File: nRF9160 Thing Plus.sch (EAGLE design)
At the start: 91 parts, among them J1 USB Female C, J10 QWIIC_RIGHT_ANGLE, J2 CON-HEADER-1X12-MALE-PIN, J3 CON-HEADER-1X16-MALE-PIN, J4 CON-1909763-1, J7 CON-1909763-1, J9 CON-0002, P1 CON-SIM-SF72S006VBAR2500, Q1 MOSFET-P-SC89, Q2 MOSFET-DUAL-COMP-SOT563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

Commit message: Updated name label and eSIM cream
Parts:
- U10: device wolff-den:IC-SIM-ST-MFF2 -> nrF9160 Thing Plus temp:IC-SIM-ST-MFF2NO_CREAM
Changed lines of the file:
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@@
 <?xml version="1.0" encoding="utf-8"?>
 <!DOCTYPE eagle SYSTEM "eagle.dtd">
-<eagle version="9.5.1">
+<eagle version="9.5.2">
 <drawing>
 <settings>
-<setting alwaysvectorfont="no"/>
+<setting alwaysvectorfont="yes"/>
 <setting keepoldvectorfont="yes"/>
 <setting verticaltext="up"/>
@@
 <layer number="128" name="_bValues" color="7" fill="1" visible="yes" active="yes"/>
 <layer number="129" name="Mask" color="7" fill="1" visible="no" active="yes"/>
+<layer number="130" name="SMDSTROOK" color="7" fill="1" visible="no" active="no"/>
 <layer number="131" name="tAdjust" color="7" fill="1" visible="no" active="yes"/>
 <layer number="132" name="bAdjust" color="7" fill="1" visible="no" active="yes"/>
+<layer number="133" name="bottom_silk" color="7" fill="1" visible="no" active="no"/>
+<layer number="134" name="mbFinish" color="7" fill="1" visible="no" active="no"/>
 <layer number="135" name="_tanames" color="7" fill="1" visible="no" active="yes"/>
 <layer number="136" name="_banames" color="7" fill="1" visible="no" active="yes"/>
 <layer number="137" name="_taDocu" color="7" fill="1" visible="no" active="yes"/>
 <layer number="138" name="_baDocu" color="7" fill="1" visible="no" active="yes"/>
+<layer number="139" name="mtKeepout" color="7" fill="1" visible="no" active="no"/>
+<layer number="140" name="mbKeepout" color="7" fill="1" visible="no" active="no"/>
+<layer number="141" name="mtRestrict" color="7" fill="1" visible="no" active="no"/>
+<layer number="142" name="mbRestrict" color="7" fill="1" visible="no" active="no"/>
+<layer number="143" name="mvRestrict" color="7" fill="1" visible="no" active="no"/>
 <layer number="144" name="Drill_legend" color="7" fill="1" visible="yes" active="yes"/>
 <layer number="145" name="DrillLegend_01-16" color="2" fill="9" visible="no" active="yes"/>
+<layer number="146" name="mMilling" color="7" fill="1" visible="no" active="no"/>
+<layer number="147" name="mMeasures" color="7" fill="1" visible="no" active="no"/>
+<layer number="148" name="mDocument" color="7" fill="1" visible="no" active="no"/>
+<layer number="149" name="mReference" color="7" fill="1" visible="no" active="no"/>
 <layer number="150" name="Notes" color="7" fill="1" visible="yes" active="yes"/>
 <layer number="151" name="HeatSink" color="7" fill="1" visible="yes" active="yes"/>
@@
 <layer number="154" name="FabDoc2" color="2" fill="1" visible="no" active="no"/>
 <layer number="155" name="FabDoc3" color="7" fill="15" visible="no" active="no"/>
+<layer number="191" name="mNets" color="7" fill="1" visible="no" active="no"/>
+<layer number="192" name="mBusses" color="7" fill="1" visible="no" active="no"/>
+<layer number="193" name="mPins" color="7" fill="1" visible="no" active="no"/>
+<layer number="194" name="mSymbols" color="7" fill="1" visible="no" active="no"/>
+<layer number="195" name="mNames" color="7" fill="1" visible="no" active="no"/>
+<layer number="196" name="mValues" color="7" fill="1" visible="no" active="no"/>
 <layer number="199" name="Contour" color="7" fill="1" visible="yes" active="yes"/>
 <layer number="200" name="200bmp" color="1" fill="10" visible="yes" active="yes"/>
@@
 <layer number="255" name="routoute" color="7" fill="1" visible="yes" active="yes"/>
 </layers>
-<schematic xreflabel="%F%N/%S.%C%R" xrefpart="/%S.%C%R">
+<schematic xreflabel="%F%N/%S" xrefpart="/%S.%C%R">
 <attributes>
 <attribute name="AUTHOR" value="Jared Wolff"/>
@@
 <part name="U7" library="wolff-den" library_urn="urn:adsk.eagle:library:6370453" deviceset="IC-NX3DV2567GU" device=""/>
 <part name="GND47" library="supply1" library_urn="urn:adsk.eagle:library:371" deviceset="GND" device=""/>
-<part name="U10" library="wolff-den" library_urn="urn:adsk.eagle:library:6370453" deviceset="IC-SIM-ST-MFF2" device=""/>
+<part name="U10" library="nrF9160 Thing Plus temp" deviceset="IC-SIM-ST-MFF2" device="NO_CREAM" value="IC-SIM-ST-MFF2"/>
 <part name="GND48" library="supply1" library_urn="urn:adsk.eagle:library:371" deviceset="GND" device=""/>
 <part name="U11" library="wolff-den" library_urn="urn:adsk.eagle:library:6370453" deviceset="IC-EMIF03-SIM02M8" device=""/>

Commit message: Moved components to local libraries
Parts not in SFE Eagle libraries were moved to local temporary libraries with the SFE SKUs added for the BOM
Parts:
- C1, C2: device wolff-den:CAP-15P-50V-0402 -> nRF9160-Capacitors:CAP-15P-50V-0402
- C10, C13, C15, C3, C8, C9: device wolff-den:CAP-4.7U-6.3V-2-0603 -> nRF9160-Capacitors:CAP-4.7U-6.3V-2-0603
- C11: device wolff-den:CAP-1U-25V-1-0402 -> nRF9160-Capacitors:CAP-1U-25V-1-0402
- C12, C19: device wolff-den:CAP-56PF-50V-1-0402 -> nRF9160-Capacitors:CAP-56PF-50V-0402
- C14, C16, C17, C18, C20, C6: device wolff-den:CAP-0.1U-50V-0402 -> nRF9160-Capacitors:CAP-0.1U-50V-0402
- C4, C5, C7: device wolff-den:CAP-10U-6.3V-0603 -> nRF9160-Capacitors:CAP-10U-6.3V-0603
- J4, J7: device wolff-den:CON-1909763-1 -> nRF9160-Connectors:CON-1909763-1
- L1: device wolff-den:IND-39NH-250MA-0402 -> nRF9160-Coils:IND-39NH-250MA-0402
- L2: device wolff-den:IND-1.5U-1.4A-2X2 -> nRF9160-Coils:IND-1.5U-1.4A-2X2
- L4: device wolff-den:IND-68NH-200MA-0402 -> nRF9160-Coils:IND-68NH-200MA-0402
- P1: device wolff-den:CON-SIM-SF72S006VBAR2500 -> nRF9160-Connectors:CON-SIM-SF72S006VBAR2500
- Q1: device wolff-den:MOSFET-P-SC89 -> nRF9160-DiscreteSemi:MOSFET-P-SC89
- Q2: device wolff-den:MOSFET-DUAL-COMP-SOT563 -> nRF9160-DiscreteSemi:MOSFET-DUAL-COMP-SOT563
- Q3: device wolff-den:MOSFET-P-20V-4.7A-SOT23 -> nRF9160-DiscreteSemi:MOSFET-P-20V-4.7A-SOT23
- Q4, Q5: device wolff-den:MOSFET-N-SC89 -> nRF9160-DiscreteSemi:MOSFET-N-SC89
- R1, R10, R13, R23, R3, R5, R6, R7, R8: device wolff-den:RES-100K-1%-0402 -> nRF9160-Resistors:RES-100K-1%-0402
- R11, R14: device wolff-den:RES-330-5%-0402 -> nRF9160-Resistors:RES-330-5%-0402
- R12: device wolff-den:RES-2K-1%-0402 -> nRF9160-Resistors:RES-2K-1%-0402
- R15: device wolff-den:RES-22K-1%-0402 -> nRF9160-Resistors:RES-22K-1%-0402
- R16: device wolff-den:RES-33K-1%-0402 -> nRF9160-Resistors:RES-33K-1%-0402
- R17, R18: device wolff-den:RES-10K-1%-0402 -> nRF9160-Resistors:RES-10K-1%-0402
- R19, R2, R22, R9: device wolff-den:RES-1M-5%-0402 -> nRF9160-Resistors:RES-1M-5%-0402
- R4: device wolff-den:RES-1K-5%-0402 -> nRF9160-Resistors:RES-1K-5%-0402
- U1: device wolff-den:MOD-NRF9160-SICA-R -> nRF9160-IC:MOD-NRF9160-SICA-R
- U11: device wolff-den:IC-EMIF03-SIM02M8 -> nRF9160-IC:IC-EMIF03-SIM02M8
- U12: device wolff-den:IC-LIS2DH12TR -> nRF9160-IC:IC-LIS2DH12TR
- U3: device wolff-den:IC-TPS63031DSKR -> nRF9160-IC:IC-TPS63031DSKR
- U4: device wolff-den:POWER-SWITCH-MIC94092YC6 -> nRF9160-IC:POWER-SWITCH-MIC94092YC6
- U5: device wolff-den:IC-CP2102N-A02-GQFN24R -> nRF9160-IC:IC-CP2102N-A02-GQFN24R
- U6: value FLASH-W25Q16JVZPIQ-WSON -> FLASH-W25Q128JVPIM-WSON; device wolff-den:FLASH-W25Q16JVZPIQ-WSON -> nRF9160-IC:FLASH-W25Q128JVPIM-WSON
- U7: device wolff-den:IC-NX3DV2567GU -> nRF9160-IC:IC-NX3DV2567GU
- U8: device wolff-den:IC-PCF85063ATL/1 -> nRF9160-IC:IC-PCF85063ATL/1
- U9: device wolff-den:IC-BAV70S -> nRF9160-DiscreteSemi:IC-BAV70S
- Y1: device wolff-den:XTAL-ABS07AIG-32.768KHZ-7-T -> nRF9160-Clocks:XTAL-ABS07AIG-32.768KHZ-7-T

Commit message: Adding Cortex-m header. Removing tag connect. Removing external SIM bits. Changing SIM holder to cheaper variant.
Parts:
- removed C18: 0.1u, nRF9160-Capacitors:CAP-0.1U-50V-0402
- removed J9: CON-0002, wolff-den:CON-0002
- removed P1: CON-SIM-SF72S006VBAR2500, nRF9160-Connectors:CON-SIM-SF72S006VBAR2500
- removed R22: 1M, nRF9160-Resistors:RES-1M-5%-0402
- removed SOLDER1: SOLDER-PASTE-ROOM-TEMP-50G, wolff-den:SOLDER-PASTE-ROOM-TEMP-50G
- removed U$34: FIDUCIAL-1MM, wolff-den:FIDUCIAL-1MM
- removed U10: IC-SIM-ST-MFF2, nrF9160 Thing Plus temp:IC-SIM-ST-MFF2NO_CREAM
- removed U11: IC-EMIF03-SIM02M8, nRF9160-IC:IC-EMIF03-SIM02M8
- removed U7: IC-NX3DV2567GU, nRF9160-IC:IC-NX3DV2567GU
- added J6: CON-SIM-104224-0820, wolff-den:CON-SIM-104224-0820
- added J8: CON-FTSH-105-XX-X-DV, wolff-den:CON-FTSH-105-XX-X-DV
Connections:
- removed net SIM_EMB_CLK: U10.CLK, U7.3Y1
- removed net SIM_EMB_IO: U10.I/O, U7.4Y1
- removed net SIM_EMB_RST: U10.RST, U7.2Y1
- removed net SIM_EMB_VCC: U10.VCC, U7.1Y1
- removed net SIM_HLDR_CLK: U11.CLKIN, U7.3Y0
- removed net SIM_HLDR_CLK_F: P1.CLK, U11.CLKEXT
- removed net SIM_HLDR_IO: U11.DATAIN, U7.4Y0
- removed net SIM_HLDR_IO_F: P1.I/O, U11.DATAEXT
- removed net SIM_HLDR_RST: U11.RSTIN, U7.2Y0
- removed net SIM_HLDR_RST_F: P1.RST, U11.RSTEXT
- removed net SIM_HLDR_VCC: P1.VCC, U11.VCC, U7.1Y0
- net +3V3: now also J8.VCC; no longer J9.VCC
- net GND: now also J6.GND, J8.GND; no longer C18.2, J9.GND, P1.DSW, P1.GND, P1.SHIELD, U10.EPAD, U10.GND, U11.GND, U7.GND
- net SIM_CLK: now also J6.CLK; no longer U7.3Z
- net SIM_DET: no longer P1.CSW, R22.2, U7.IN
- net SIM_IO: now also J6.I/O; no longer U7.4Z
- net SIM_RST: now also J6.RST; no longer U7.2Z
- net SIM_VCC: now also J6.VCC; no longer C18.1, R22.1, U7.1Z, U7.VCC
- net SWCLK: now also J8.SWDCLK; no longer J9.SWCLK
- net SWDIO: now also J8.SWDIO; no longer J9.SWDIO
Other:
- note added: "Nano SIM"
- note removed: "SIMs"
- moved on the sheet: TP1, TP2

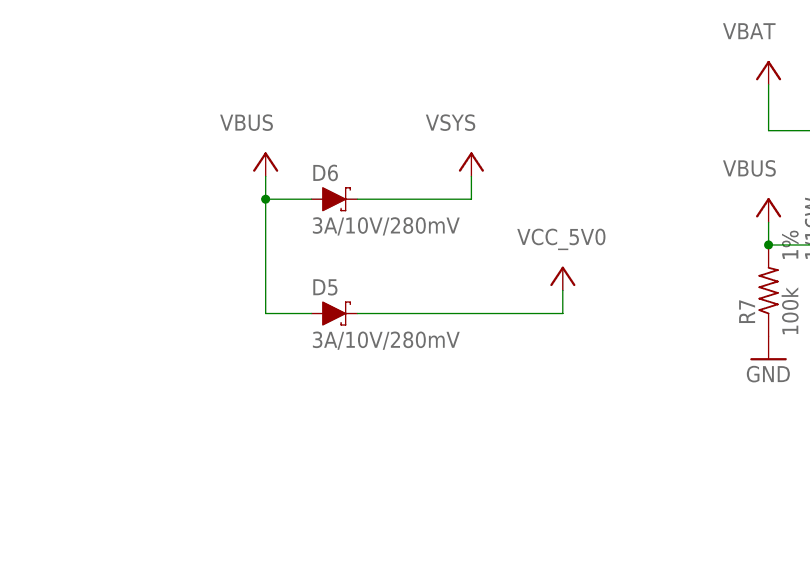
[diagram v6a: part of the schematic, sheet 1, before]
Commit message: Changing flash to W25Q32JVZPIQ. Changing D5/6 to BAT20J.
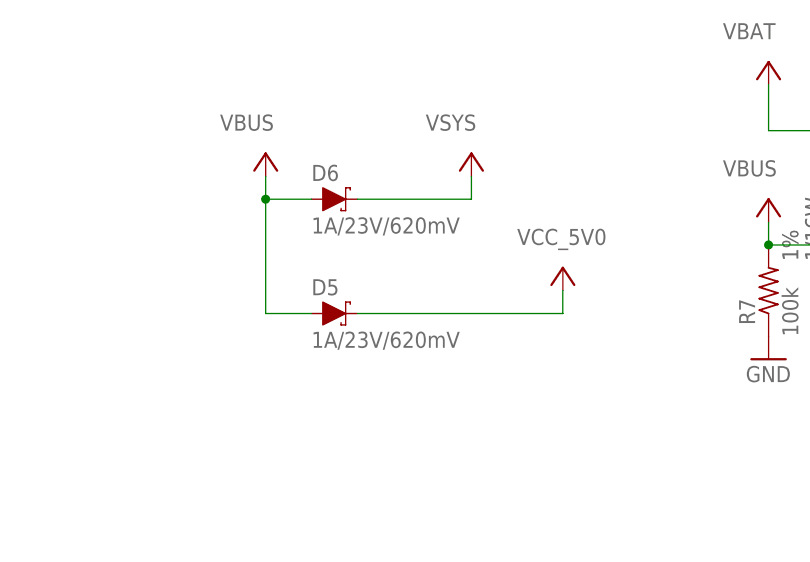
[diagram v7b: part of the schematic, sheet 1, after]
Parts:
- D5, D6: value 3A/10V/280mV -> 1A/23V/620mV; device SparkFun-DiscreteSemi:DIODE-SCHOTTKY-BAT60A -> SparkFun-DiscreteSemi:DIODE-SCHOTTKY-BAT20J
- U6: value FLASH-W25Q128JVPIM-WSON -> FLASH-WSON; device nRF9160-IC:FLASH-W25Q128JVPIM-WSON -> wolff-den:FLASH-W25Q32JVZPIQ-WSON
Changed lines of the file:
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@@
 <?xml version="1.0" encoding="utf-8"?>
 <!DOCTYPE eagle SYSTEM "eagle.dtd">
-<eagle version="9.5.1">
+<eagle version="9.6.2">
 <drawing>
 <settings>
@@
 <part name="SW2" library="SparkFun-Switches" deviceset="MOMENTARY-SWITCH-SPST" device="-SMD-4.6X2.8MM"/>
 <part name="GND13" library="supply1" library_urn="urn:adsk.eagle:library:371" deviceset="GND" device=""/>
-<part name="U6" library="nRF9160-IC" deviceset="FLASH" device="-WSON" package3d_urn="urn:adsk.eagle:package:19416409/2" override_package3d_urn="urn:adsk.eagle:package:19415944/2" override_package_urn="urn:adsk.eagle:footprint:19415945/1" override_locally_modified="yes" technology="-W25Q128JVPIM" value="FLASH-W25Q128JVPIM-WSON"/>
+<part name="U6" library="wolff-den" library_urn="urn:adsk.eagle:library:6370453" deviceset="FLASH" device="-WSON" package3d_urn="urn:adsk.eagle:package:19416409/2" override_package3d_urn="urn:adsk.eagle:package:19415944/2" override_package_urn="urn:adsk.eagle:footprint:19415945/1" override_locally_modified="yes" technology="-W25Q32JVZPIQ" value="FLASH-WSON"/>
 <part name="GND15" library="supply1" library_urn="urn:adsk.eagle:library:371" deviceset="GND" device=""/>
 <part name="+3V7" library="supply1" library_urn="urn:adsk.eagle:library:371" deviceset="+3V3" device=""/>
@@
 <part name="U5" library="nRF9160-IC" deviceset="IC-CP2102N-A02-GQFN24R" device=""/>
 <part name="J5" library="SparkFun-Connectors" library_urn="urn:adsk.eagle:library:513" deviceset="JST_2MM_MALE" device="" package3d_urn="urn:adsk.eagle:package:38042/1"/>
-<part name="D5" library="SparkFun-DiscreteSemi" deviceset="DIODE-SCHOTTKY" device="-BAT60A" value="3A/10V/280mV"/>
-<part name="D6" library="SparkFun-DiscreteSemi" deviceset="DIODE-SCHOTTKY" device="-BAT60A" value="3A/10V/280mV"/>
+<part name="D5" library="SparkFun-DiscreteSemi" deviceset="DIODE-SCHOTTKY" device="-BAT20J" value="1A/23V/620mV"/>
+<part name="D6" library="SparkFun-DiscreteSemi" deviceset="DIODE-SCHOTTKY" device="-BAT20J" value="1A/23V/620mV"/>
 <part name="U12" library="nRF9160-IC" deviceset="IC-LIS2DH12TR" device="" package3d_urn="urn:adsk.eagle:package:5807341/2" override_package3d_urn="urn:adsk.eagle:package:5807341/3" override_package_urn="urn:adsk.eagle:footprint:5807301/2"/>
 <part name="SUPPLY3" library="supply2" library_urn="urn:adsk.eagle:library:372" deviceset="GND" device=""/>

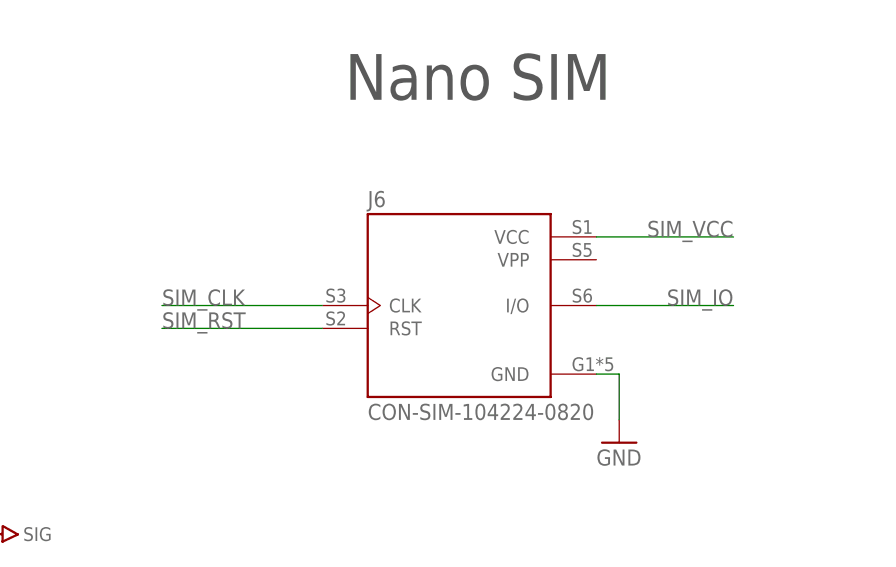
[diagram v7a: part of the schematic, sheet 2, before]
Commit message: Adding test points for SIM
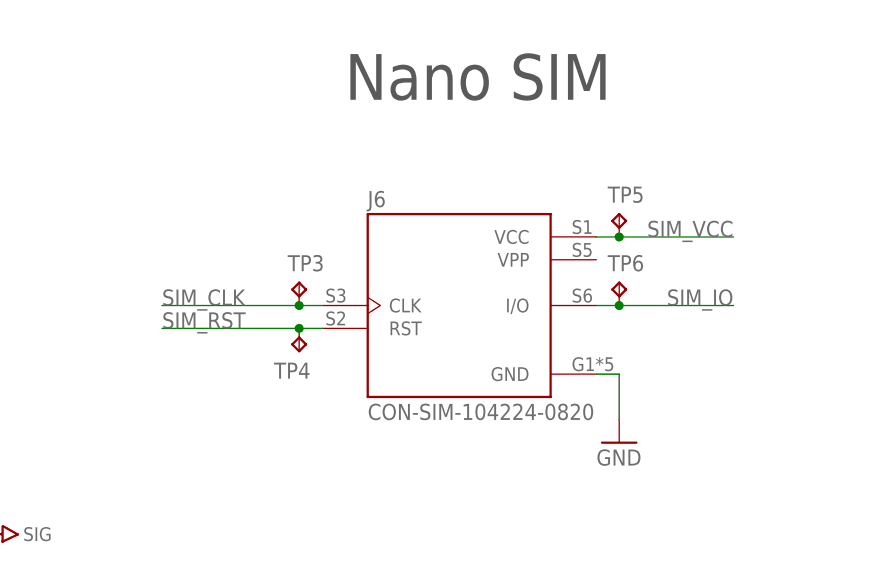
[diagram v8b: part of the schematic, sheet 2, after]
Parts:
- added TP3, TP4, TP5, TP6: TP-1SIDE-1P0, wolff-den:TP-1SIDE-1P0
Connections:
- net SIM_CLK: now also TP3.TP
- net SIM_IO: now also TP6.TP
- net SIM_RST: now also TP4.TP
- net SIM_VCC: now also TP5.TP
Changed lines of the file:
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@@
 <part name="GND32" library="supply1" library_urn="urn:adsk.eagle:library:371" deviceset="GND" device=""/>
 <part name="J6" library="wolff-den" library_urn="urn:adsk.eagle:library:6370453" deviceset="CON-SIM" device="" package3d_urn="urn:adsk.eagle:package:19415237/3" technology="-104224-0820"/>
+<part name="TP3" library="wolff-den" library_urn="urn:adsk.eagle:library:6370453" deviceset="TP" device="-1SIDE-1P0" package3d_urn="urn:adsk.eagle:package:24898411/1"/>
+<part name="TP4" library="wolff-den" library_urn="urn:adsk.eagle:library:6370453" deviceset="TP" device="-1SIDE-1P0" package3d_urn="urn:adsk.eagle:package:24898411/1"/>
+<part name="TP5" library="wolff-den" library_urn="urn:adsk.eagle:library:6370453" deviceset="TP" device="-1SIDE-1P0" package3d_urn="urn:adsk.eagle:package:24898411/1"/>
+<part name="TP6" library="wolff-den" library_urn="urn:adsk.eagle:library:6370453" deviceset="TP" device="-1SIDE-1P0" package3d_urn="urn:adsk.eagle:package:24898411/1"/>
 </parts>
 <sheets>
@@
 <attribute name="VALUE" x="358.1304" y="208.268" size="1.77968125" layer="96"/>
 </instance>
+<instance part="TP3" gate="G$1" x="350.52" y="223.52" smashed="yes">
+<attribute name="NAME" x="349.25" y="224.79" size="1.778" layer="95"/>
+</instance>
+<instance part="TP4" gate="G$1" x="350.52" y="215.9" smashed="yes" rot="R180">
+<attribute name="NAME" x="351.79" y="214.63" size="1.778" layer="95" rot="R180"/>
+</instance>
+<instance part="TP5" gate="G$1" x="386.08" y="231.14" smashed="yes">
+<attribute name="NAME" x="384.81" y="232.41" size="1.778" layer="95"/>
+</instance>
+<instance part="TP6" gate="G$1" x="386.08" y="223.52" smashed="yes">
+<attribute name="NAME" x="384.81" y="224.79" size="1.778" layer="95"/>
+</instance>
 </instances>
 <busses>
@@
 </segment>
 <segment>
-<wire x1="353.06" y1="220.98" x2="335.28" y2="220.98" width="0.1524" layer="91"/>
+<wire x1="353.06" y1="220.98" x2="350.52" y2="220.98" width="0.1524" layer="91"/>
 <label x="335.28" y="220.98" size="1.778" layer="95"/>
 <pinref part="J6" gate="G$1" pin="CLK"/>
+<pinref part="TP3" gate="G$1" pin="TP"/>
+<wire x1="350.52" y1="220.98" x2="335.28" y2="220.98" width="0.1524" layer="91"/>
+<junction x="350.52" y="220.98"/>
 </segment>
 </net>
@@
 </segment>
 <segment>
-<wire x1="353.06" y1="218.44" x2="335.28" y2="218.44" width="0.1524" layer="91"/>
+<wire x1="353.06" y1="218.44" x2="350.52" y2="218.44" width="0.1524" layer="91"/>
 <label x="335.28" y="218.44" size="1.778" layer="95"/>
 <pinref part="J6" gate="G$1" pin="RST"/>
+<pinref part="TP4" gate="G$1" pin="TP"/>
+<wire x1="350.52" y1="218.44" x2="335.28" y2="218.44" width="0.1524" layer="91"/>
+<junction x="350.52" y="218.44"/>
 </segment>
 </net>
@@
 <segment>
 <label x="398.78" y="220.98" size="1.778" layer="95" rot="MR0"/>
-<wire x1="383.54" y1="220.98" x2="398.78" y2="220.98" width="0.1524" layer="91"/>
+<wire x1="383.54" y1="220.98" x2="386.08" y2="220.98" width="0.1524" layer="91"/>
 <pinref part="J6" gate="G$1" pin="I/O"/>
+<pinref part="TP6" gate="G$1" pin="TP"/>
+<wire x1="386.08" y1="220.98" x2="398.78" y2="220.98" width="0.1524" layer="91"/>
+<junction x="386.08" y="220.98"/>
 </segment>
 </net>
@@
 </segment>
 <segment>
-<wire x1="383.54" y1="228.6" x2="398.78" y2="228.6" width="0.1524" layer="91"/>
+<wire x1="383.54" y1="228.6" x2="386.08" y2="228.6" width="0.1524" layer="91"/>
 <label x="398.78" y="228.6" size="1.778" layer="95" rot="MR0"/>
 <pinref part="J6" gate="G$1" pin="VCC"/>
-</segment>
-</net>
+<pinref part="TP5" gate="G$1" pin="TP"/>
+<wire x1="386.08" y1="228.6" x2="398.78" y2="228.6" width="0.1524" layer="91"/>
+<junction x="386.08" y="228.6"/>
+</segment>
+</net>
